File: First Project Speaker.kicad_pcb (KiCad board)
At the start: 2 copper layers, 46.4 x 52.1 mm, 54 parts, among them J1 USB_C_Receptacle_USB2.0_16P, J2 Screw_Terminal_01x02, J3 Screw_Terminal_01x02, SW1 SW_Push, SW2 SW_Push, SW3 SW_Push, U1 LD1117S33TR_SOT223, U2 PCM2704CDBR, U3 TDA7297, U4 CH221K, Y1 12M

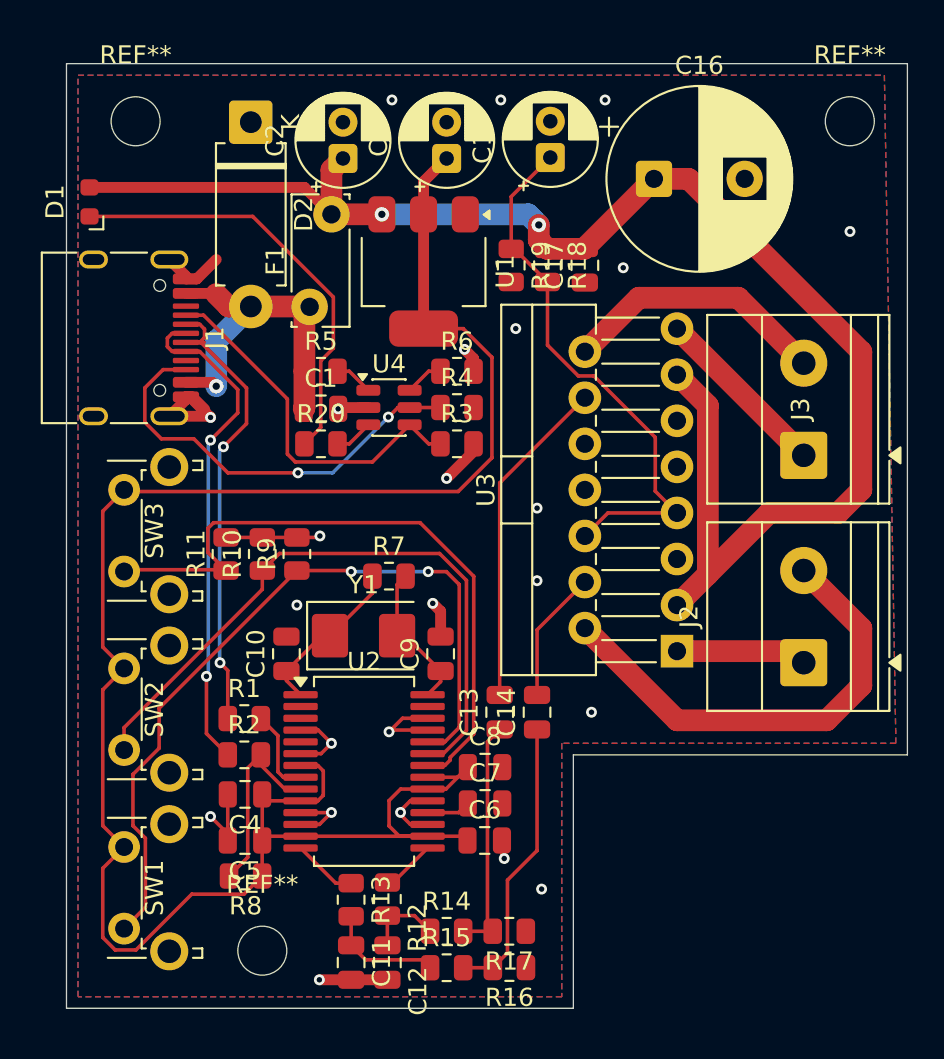
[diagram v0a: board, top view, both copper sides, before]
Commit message: V3: add J4 screw terminal for external audio visualizer PCB, extend board outline, V3 renders
Co-Authored-By: Claude Fable 5 <noreply@anthropic.com>
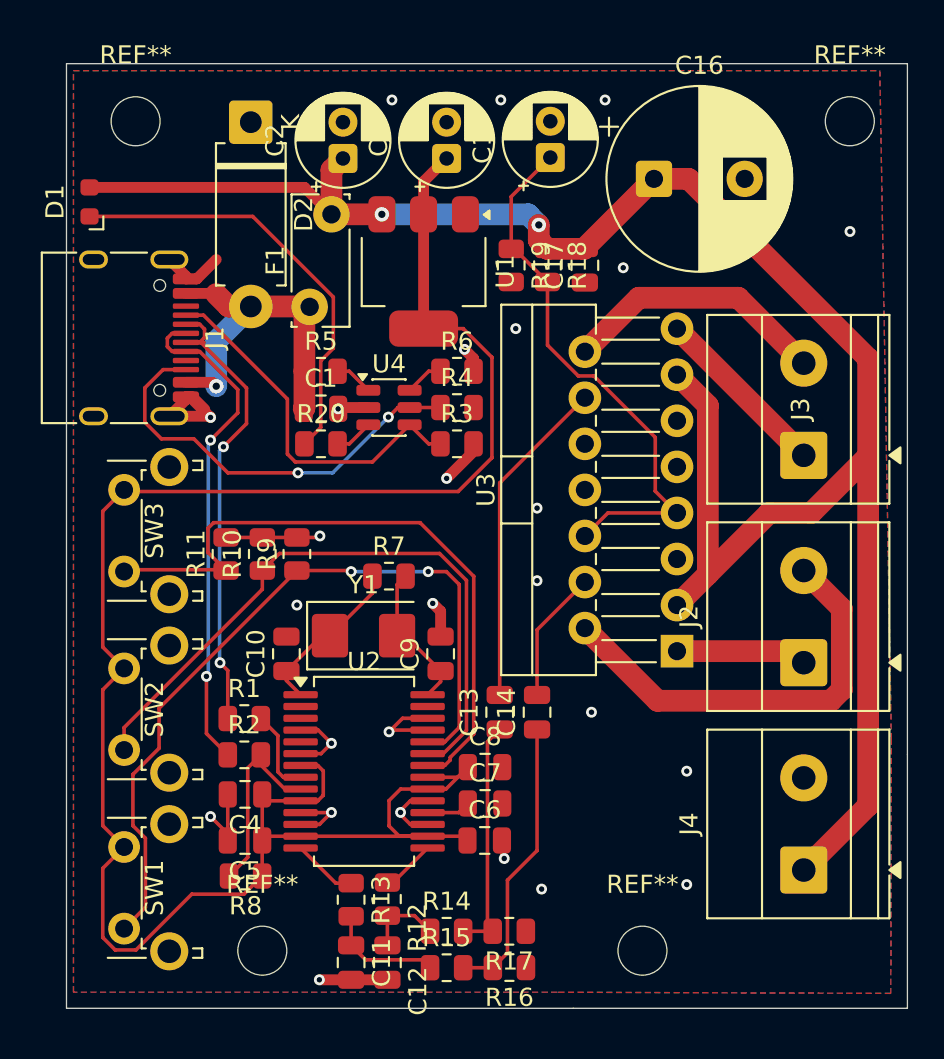
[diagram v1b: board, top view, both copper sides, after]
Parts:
- added J4: Screw_Terminal_01x02, TerminalBlock_Phoenix:TerminalBlock_Phoenix_MKDS-1,5-2-5.08_1x02_P5.08mm_Horizontal, F.Cu at (108.0, 76.2)
- added REF**: MountingHole_2.7mm_M2.5, MountingHole:MountingHole_2.7mm_M2.5, F.Cu at (99.1, 80.6)
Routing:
- net /+12V: track 85.4 -> 109.2 mm
- net /OUT_L-: track 25.8 -> 23.5 mm
- net GND: vias 24 -> 26
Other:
- outline, holes or cut-outs redrawn
